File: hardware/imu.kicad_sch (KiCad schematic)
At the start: 3 parts, among them U9 LSM6DSV16XTR

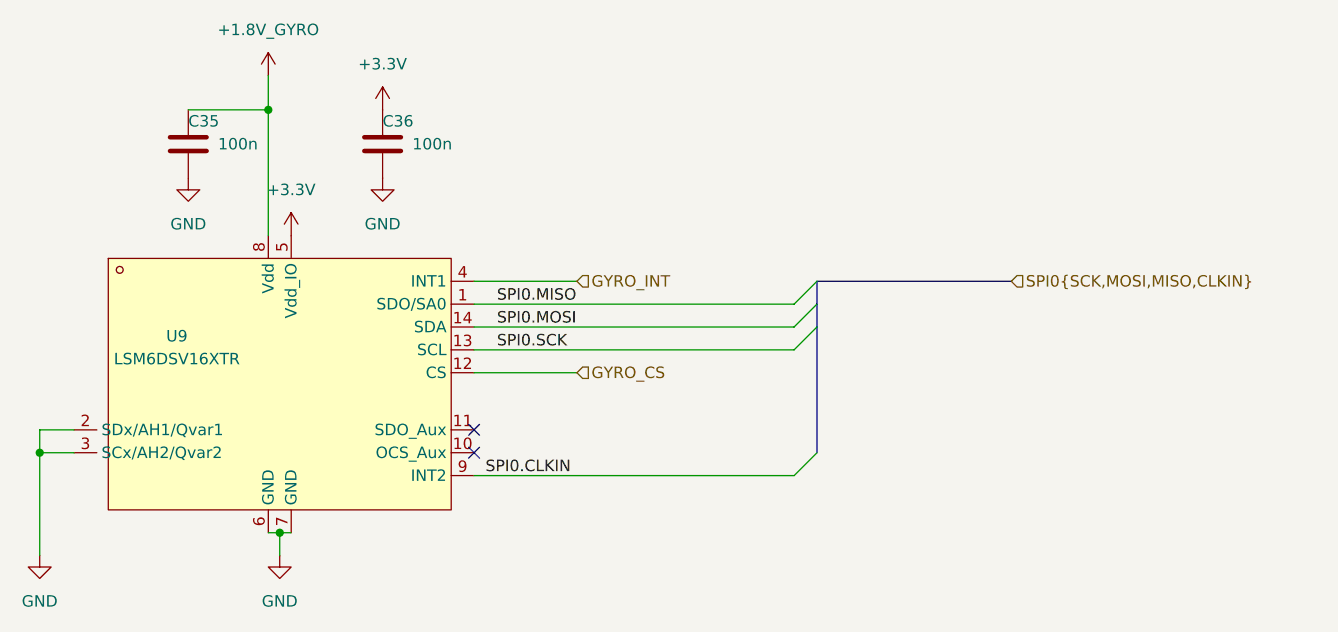
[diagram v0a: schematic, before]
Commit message: many tiny improvements
- I/O correctness
- SPI0/SPI1/I2C0 bus corrections
- decoupling of DVDD
- ADC_AVDD as per RPi documents
- removal of SBUS
- connect ESC serial
- remove RUN RC-circuit as per RPi documentation
- some more cleanup for readability
- gyro CLKIN decision
- I2C 4.7k pullup
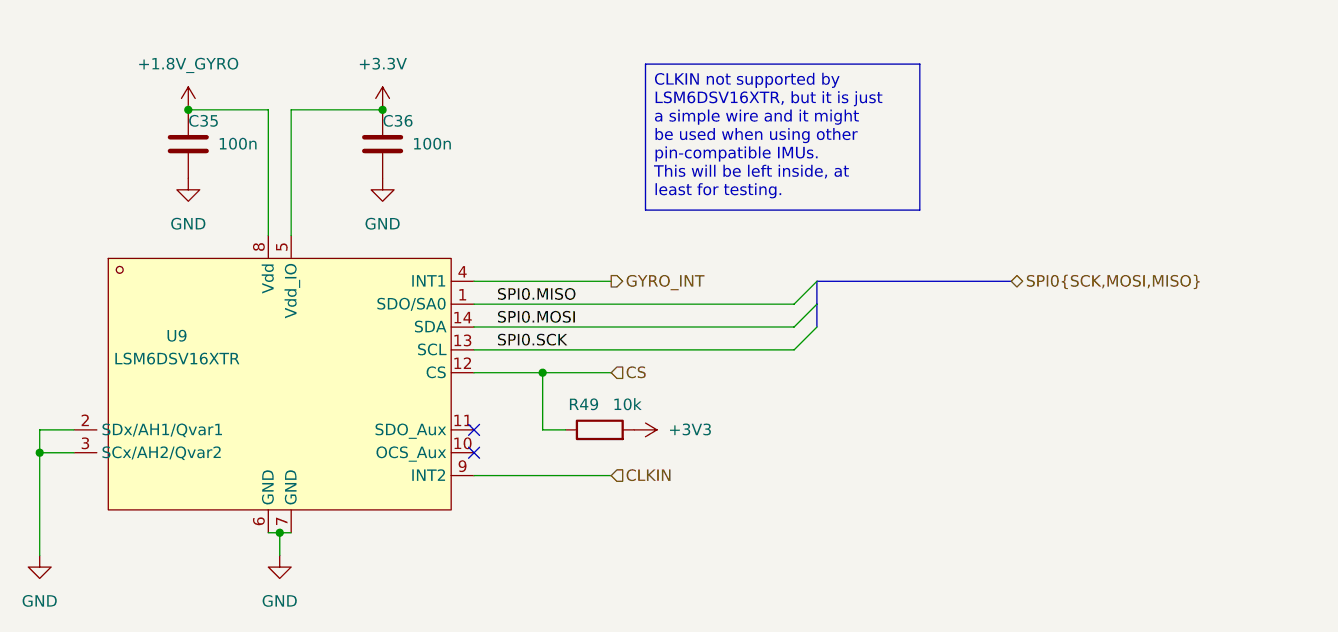
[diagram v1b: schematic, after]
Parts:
- added R49: 10k, Resistor_SMD:R_0201_0603Metric, symbol Device:R
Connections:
- net GYRO_CS renamed CS
- net CS: now also R49.1
- net SPI0.CLKIN renamed CLKIN
- new net +3V3: R49.2

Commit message: RP2354A
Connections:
- net +3V3 is gone; now on net +3.3V: R49.2
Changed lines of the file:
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@@
+	)
+	(symbol
+		(lib_id "power:+3.3V")
+		(at 111.76 78.74 270)
+		(unit 1)
+		(body_style 1)
+		(exclude_from_sim no)
+		(in_bom yes)
+		(on_board yes)
+		(in_pos_files yes)
+		(dnp no)
+		(fields_autoplaced yes)
+		(property "Reference" "#PWR0156"
+			(at 107.95 78.74 0)
+			(hide yes)
+			(show_name no)
+			(do_not_autoplace no)
+			(effects
+				(font
+					(size 1.27 1.27)
+				)
+			)
+		)
+		(property "Value" "+3.3V"
+			(at 115.57 78.7399 90)
+			(show_name no)
+			(do_not_autoplace no)
+			(effects
+				(font
+					(size 1.27 1.27)
+				)
+				(justify left)
+			)
+		)
+		(property "Footprint" ""
+			(at 111.76 78.74 0)
+			(hide yes)
+			(show_name no)
+			(do_not_autoplace no)
+			(effects
+				(font
+					(size 1.27 1.27)
+				)
+			)
+		)
+		(property "Datasheet" ""
+			(at 111.76 78.74 0)
+			(hide yes)
+			(show_name no)
+			(do_not_autoplace no)
+			(effects
+				(font
+					(size 1.27 1.27)
+				)
+			)
+		)
+		(property "Description" "Power symbol creates a global label with name \"+3.3V\""
+			(at 111.76 78.74 0)
+			(hide yes)
+			(show_name no)
+			(do_not_autoplace no)
+			(effects
+				(font
+					(size 1.27 1.27)
+				)
+			)
+		)
+		(pin "1"
+		)
+		(instances
+			(project "OpenFC"
+				(path "/fb88b6f9-ee39-4640-a9d4-04a17ceeac64/757ed1e6-9a5f-4a0e-a946-254eae8dfb0d"
+					(reference "#PWR0156")
+					(unit 1)
+				)
+			)
+		)
 	)
 	(symbol
@@
 					(unit 1)
 				)
-			)
-		)
-	)
-	(symbol
-		(lib_id "power:+3V3")
-		(at 111.76 78.74 270)
-		(unit 1)
-		(body_style 1)
-		(exclude_from_sim no)
-		(in_bom yes)
-		(on_board yes)
-		(in_pos_files yes)
-		(dnp no)
-		(fields_autoplaced yes)
-		(property "Reference" "#PWR07"
-			(at 107.95 78.74 0)
-			(hide yes)
-			(show_name no)
-			(do_not_autoplace no)
-			(effects
-				(font
-					(size 1.27 1.27)
-				)
-			)
-		)
-		(property "Value" "+3V3"
-			(at 115.57 78.7399 90)
-			(show_name no)
-			(do_not_autoplace no)
-			(effects
-				(font
-					(size 1.27 1.27)
-				)
-				(justify left)
-			)
-		)
-		(property "Footprint" ""
-			(at 111.76 78.74 0)
-			(hide yes)
-			(show_name no)
-			(do_not_autoplace no)
-			(effects
-				(font
-					(size 1.27 1.27)
-				)
-			)
-		)
-		(property "Datasheet" ""
-			(at 111.76 78.74 0)
-			(hide yes)
-			(show_name no)
-			(do_not_autoplace no)
-			(effects
-				(font
-					(size 1.27 1.27)
-				)
-			)
-		)
-		(property "Description" "Power symbol creates a global label with name \"+3V3\""
-			(at 111.76 78.74 0)
-			(hide yes)
-			(show_name no)
-			(do_not_autoplace no)
-			(effects
-				(font
-					(size 1.27 1.27)
-				)
-			)
-		)
-		(pin "1"
-		)
-		(instances
-			(project "OpenFC"
-				(path "/fb88b6f9-ee39-4640-a9d4-04a17ceeac64/757ed1e6-9a5f-4a0e-a946-254eae8dfb0d"
-					(reference "#PWR07")
-					(unit 1)
-				)
